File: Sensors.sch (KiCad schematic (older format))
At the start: 0 parts

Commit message: Added Polyfuses and replace diodes
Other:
- note removed: "Gniazdo USB B\nSWD\nUART"
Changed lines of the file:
@@
 $Descr A4 11693 8268
 encoding utf-8
-Sheet 7 10
+Sheet 10 10
 Title ""
 Date ""
@@
 Comment4 ""
 $EndDescr
-Text Notes 1300 1250 0    50   ~ 0
-Gniazdo USB B\nSWD\nUART
 $EndSCHEMATC

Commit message: Numbering and finishing the schematic
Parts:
- added C66: 0.1uF, symbol Device:C
- added R72, R73: 2.2kΩ, symbol Device:R
- added U10: SHTC3, footprints:DFN-4-1EP_2x2mm_P1mm_EP0.7x1.6mm, symbol Library:SHTC3
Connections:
- new net +3V3: C66.1, R72.1, R73.1, U10.1 (VDD)
- new net GND: C66.2, U10.4 (VSS)
- new net I2C_SCL: R73.2, U10.2 (SCL)
- new net I2C_SDA: R72.2, U10.3 (SDA)
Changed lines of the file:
@@
 Comment4 ""
 $EndDescr
+$Comp
+L Library:SHTC3 U10
+U 1 1 5E1916D2
+P 3250 2450
+F 0 "U10" H 3000 2700 50  0000 L CNN
+F 1 "SHTC3" H 3250 2700 50  0000 L CNN
+F 2 "footprints:DFN-4-1EP_2x2mm_P1mm_EP0.7x1.6mm" H 3050 2200 50  0001 C CNN
+F 3 "" H 3050 2200 50  0001 C CNN
+	1    3250 2450
+	1    0    0    -1
+$EndComp
+$Comp
+L Device:C C66
+U 1 1 5E15E1F1
+P 3900 2450
+F 0 "C66" H 4015 2496 50  0000 L CNN
+F 1 "0.1uF" H 4015 2405 50  0000 L CNN
+F 2 "" H 3938 2300 50  0001 C CNN
+F 3 "~" H 3900 2450 50  0001 C CNN
+	1    3900 2450
+	1    0    0    -1
+$EndComp
+$Comp
+L power:GND #PWR0177
+U 1 1 5E15EB06
+P 3900 2700
+F 0 "#PWR0177" H 3900 2450 50  0001 C CNN
+F 1 "GND" H 3905 2527 50  0000 C CNN
+F 2 "" H 3900 2700 50  0001 C CNN
+F 3 "" H 3900 2700 50  0001 C CNN
+	1    3900 2700
+	1    0    0    -1
+$EndComp
+$Comp
+L power:+3.3V #PWR0176
+U 1 1 5E15FDB5
+P 3900 1650
+F 0 "#PWR0176" H 3900 1500 50  0001 C CNN
+F 1 "+3.3V" H 3915 1823 50  0000 C CNN
+F 2 "" H 3900 1650 50  0001 C CNN
+F 3 "" H 3900 1650 50  0001 C CNN
+	1    3900 1650
+	1    0    0    -1
+$EndComp
+Wire Wire Line
+	3900 1650 3900 1750
+Wire Wire Line
+	3900 2250 3700 2250
+Wire Wire Line
+	3700 2250 3700 2400
+Wire Wire Line
+	3700 2400 3650 2400
+Connection ~ 3900 2250
+Wire Wire Line
+	3900 2250 3900 2300
+Wire Wire Line
+	3650 2500 3700 2500
+Wire Wire Line
+	3700 2500 3700 2650
+Wire Wire Line
+	3700 2650 3900 2650
+Wire Wire Line
+	3900 2650 3900 2600
+Wire Wire Line
+	3900 2700 3900 2650
+Connection ~ 3900 2650
+Wire Wire Line
+	2850 2400 2600 2400
+Wire Wire Line
+	2850 2500 2250 2500
+Text GLabel 2100 2400 0    50   Input ~ 0
+I2C_SCL
+Text GLabel 2100 2500 0    50   BiDi ~ 0
+I2C_SDA
+$Comp
+L Device:R R?
+U 1 1 5E1C6F9E
+P 2600 2100
+AR Path="/5E91D7CC/5E1C6F9E" Ref="R?"  Part="1"
+AR Path="/5E91D96F/5E1C6F9E" Ref="R?"  Part="1"
+AR Path="/5E1B3A8F/5E1C6F9E" Ref="R73"  Part="1"
+F 0 "R73" H 2670 2146 50  0000 L CNN
+F 1 "2.2kΩ" H 2670 2055 50  0000 L CNN
+F 2 "" V 2530 2100 50  0001 C CNN
+F 3 "~" H 2600 2100 50  0001 C CNN
+	1    2600 2100
+	1    0    0    -1
+$EndComp
+$Comp
+L Device:R R?
+U 1 1 5E1C6FA4
+P 2250 2100
+AR Path="/5E91D7CC/5E1C6FA4" Ref="R?"  Part="1"
+AR Path="/5E91D96F/5E1C6FA4" Ref="R?"  Part="1"
+AR Path="/5E1B3A8F/5E1C6FA4" Ref="R72"  Part="1"
+F 0 "R72" H 2320 2146 50  0000 L CNN
+F 1 "2.2kΩ" H 2320 2055 50  0000 L CNN
+F 2 "" V 2180 2100 50  0001 C CNN
+F 3 "~" H 2250 2100 50  0001 C CNN
+	1    2250 2100
+	1    0    0    -1
+$EndComp
+Wire Wire Line
+	2250 2250 2250 2500
+Wire Wire Line
+	2600 1950 2600 1750
+Wire Wire Line
+	2600 1750 2250 1750
+Wire Wire Line
+	2250 1750 2250 1950
+Connection ~ 2600 1750
+Connection ~ 2250 2500
+Wire Wire Line
+	2250 2500 2100 2500
+Wire Wire Line
+	2600 2250 2600 2400
+Connection ~ 2600 2400
+Wire Wire Line
+	2600 2400 2100 2400
+Wire Wire Line
+	2600 1750 3900 1750
+Connection ~ 3900 1750
+Wire Wire Line
+	3900 1750 3900 2250
 $EndSCHEMATC

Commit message: Shematic almost finished, BOM in KiCad 3/4 finished
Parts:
- C68: renamed from C66; footprint (none) -> Capacitor_SMD:C_0603_1608Metric; Cena (none) -> 0.05982; Model (none) -> CL10B104KB8NNNC; Napięcie (none) -> 50V; Producent (none) -> SAMSUNG; Tolerancja (none) -> 10%; Typ (none) -> SMD
- R72, R73: footprint (none) -> Resistor_SMD:R_0603_1608Metric
- U10: Cena (none) -> 7.2; Link (none) -> https://www.tme.eu/pl/details/shtc3/czujniki-wilgotnosci/se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; Model (none) -> SHTC3; Opis (none) -> Czujnik: temperatury i wilgotności; Zakres: 0÷100% RH; -0,3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; Producent (none) -> SENSIRION; Typ (none) -> SMD
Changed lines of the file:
@@
 F 2 "footprints:DFN-4-1EP_2x2mm_P1mm_EP0.7x1.6mm" H 3050 2200 50  0001 C CNN
 F 3 "" H 3050 2200 50  0001 C CNN
+F 4 "7.2" H 3250 2450 50  0001 C CNN "Cena"
+F 5 "https://www.tme.eu/pl/details/shtc3/czujniki-wilgotnosci/sensirion/3-000-047/" H 3250 2450 50  0001 C CNN "Link"
+F 6 "SHTC3" H 3250 2450 50  0001 C CNN "Model"
+F 7 "Czujnik: temperatury i wilgotności; Zakres: 0÷100% RH; -0,3÷4VDC" H 3250 2450 50  0001 C CNN "Opis"
+F 8 "SENSIRION" H 3250 2450 50  0001 C CNN "Producent"
+F 9 "SMD" H 3250 2450 50  0001 C CNN "Typ"
 	1    3250 2450
 	1    0    0    -1
 $EndComp
 $Comp
-L Device:C C66
+L Device:C C68
 U 1 1 5E15E1F1
 P 3900 2450
-F 0 "C66" H 4015 2496 50  0000 L CNN
+F 0 "C68" H 4015 2496 50  0000 L CNN
 F 1 "0.1uF" H 4015 2405 50  0000 L CNN
-F 2 "" H 3938 2300 50  0001 C CNN
+F 2 "Capacitor_SMD:C_0603_1608Metric" H 3938 2300 50  0001 C CNN
 F 3 "~" H 3900 2450 50  0001 C CNN
+F 4 "0.05982" H 3900 2450 50  0001 C CNN "Cena"
+F 5 "CL10B104KB8NNNC " H 3900 2450 50  0001 C CNN "Model"
+F 6 "50V" H 3900 2450 50  0001 C CNN "Napięcie"
+F 7 "SAMSUNG" H 3900 2450 50  0001 C CNN "Producent"
+F 8 "10%" H 3900 2450 50  0001 C CNN "Tolerancja"
+F 9 "SMD" H 3900 2450 50  0001 C CNN "Typ"
 	1    3900 2450
 	1    0    0    -1
@@
 F 0 "R73" H 2670 2146 50  0000 L CNN
 F 1 "2.2kΩ" H 2670 2055 50  0000 L CNN
-F 2 "" V 2530 2100 50  0001 C CNN
+F 2 "Resistor_SMD:R_0603_1608Metric" V 2530 2100 50  0001 C CNN
 F 3 "~" H 2600 2100 50  0001 C CNN
 	1    2600 2100
@@
 F 0 "R72" H 2320 2146 50  0000 L CNN
 F 1 "2.2kΩ" H 2320 2055 50  0000 L CNN
-F 2 "" V 2180 2100 50  0001 C CNN
+F 2 "Resistor_SMD:R_0603_1608Metric" V 2180 2100 50  0001 C CNN
 F 3 "~" H 2250 2100 50  0001 C CNN
 	1    2250 2100

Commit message: BOM in KiCad almost finished, genereated NETLIST, create PCB
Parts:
- R72, R73: Cena (none) -> 0.04651; Typ (none) -> SMD
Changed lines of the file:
@@
 F 2 "Resistor_SMD:R_0603_1608Metric" V 2530 2100 50  0001 C CNN
 F 3 "~" H 2600 2100 50  0001 C CNN
+F 4 "0.04651" H 2600 2100 50  0001 C CNN "Cena"
+F 5 "SMD" H 2600 2100 50  0001 C CNN "Typ"
 	1    2600 2100
 	1    0    0    -1
@@
 F 2 "Resistor_SMD:R_0603_1608Metric" V 2180 2100 50  0001 C CNN
 F 3 "~" H 2250 2100 50  0001 C CNN
+F 4 "0.04651" H 2250 2100 50  0001 C CNN "Cena"
+F 5 "SMD" H 2250 2100 50  0001 C CNN "Typ"
 	1    2250 2100
 	1    0    0    -1

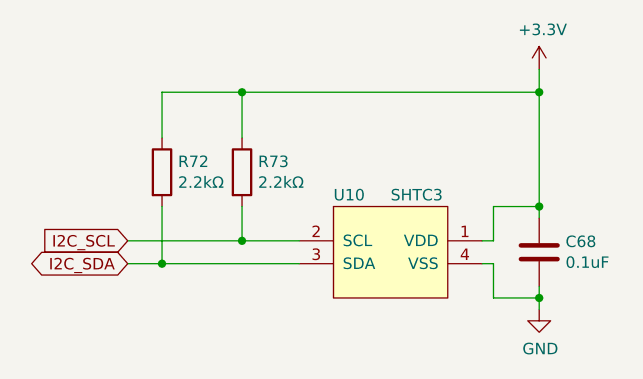
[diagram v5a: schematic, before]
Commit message: Improve Emergency, Added TVS diodes
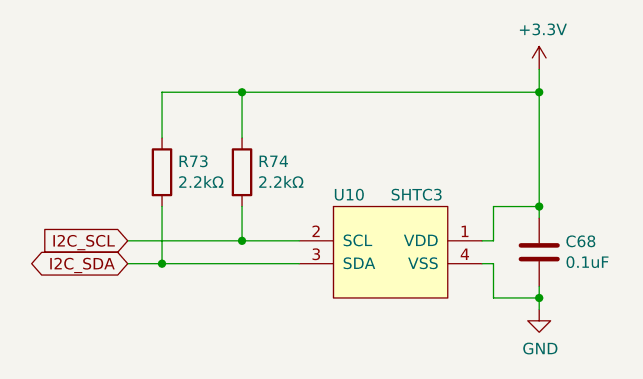
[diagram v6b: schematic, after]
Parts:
- renumbered R72 to R73, R73 to R74
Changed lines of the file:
@@
 $EndComp
 $Comp
-L power:GND #PWR0177
+L power:GND #PWR0176
 U 1 1 5E15EB06
 P 3900 2700
-F 0 "#PWR0177" H 3900 2450 50  0001 C CNN
+F 0 "#PWR0176" H 3900 2450 50  0001 C CNN
 F 1 "GND" H 3905 2527 50  0000 C CNN
 F 2 "" H 3900 2700 50  0001 C CNN
@@
 $EndComp
 $Comp
-L power:+3.3V #PWR0176
+L power:+3.3V #PWR0175
 U 1 1 5E15FDB5
 P 3900 1650
-F 0 "#PWR0176" H 3900 1500 50  0001 C CNN
+F 0 "#PWR0175" H 3900 1500 50  0001 C CNN
 F 1 "+3.3V" H 3915 1823 50  0000 C CNN
 F 2 "" H 3900 1650 50  0001 C CNN
@@
 AR Path="/5E91D7CC/5E1C6F9E" Ref="R?"  Part="1"
 AR Path="/5E91D96F/5E1C6F9E" Ref="R?"  Part="1"
-AR Path="/5E1B3A8F/5E1C6F9E" Ref="R73"  Part="1"
-F 0 "R73" H 2670 2146 50  0000 L CNN
+AR Path="/5E1B3A8F/5E1C6F9E" Ref="R74"  Part="1"
+F 0 "R74" H 2670 2146 50  0000 L CNN
 F 1 "2.2kΩ" H 2670 2055 50  0000 L CNN
 F 2 "Resistor_SMD:R_0603_1608Metric" V 2530 2100 50  0001 C CNN
@@
 AR Path="/5E91D7CC/5E1C6FA4" Ref="R?"  Part="1"
 AR Path="/5E91D96F/5E1C6FA4" Ref="R?"  Part="1"
-AR Path="/5E1B3A8F/5E1C6FA4" Ref="R72"  Part="1"
-F 0 "R72" H 2320 2146 50  0000 L CNN
+AR Path="/5E1B3A8F/5E1C6FA4" Ref="R73"  Part="1"
+F 0 "R73" H 2320 2146 50  0000 L CNN
 F 1 "2.2kΩ" H 2320 2055 50  0000 L CNN
 F 2 "Resistor_SMD:R_0603_1608Metric" V 2180 2100 50  0001 C CNN

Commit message: Added 12V regulator, aditional input, outputs, improved inputs ESD
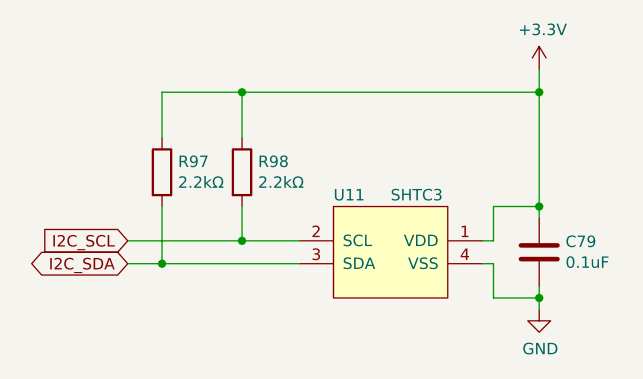
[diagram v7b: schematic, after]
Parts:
- renumbered C68 to C79, R73 to R97, R74 to R98, U10 to U11
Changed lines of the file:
@@
 $EndDescr
 $Comp
-L Library:SHTC3 U10
+L Library:SHTC3 U11
 U 1 1 5E1916D2
 P 3250 2450
-F 0 "U10" H 3000 2700 50  0000 L CNN
+F 0 "U11" H 3000 2700 50  0000 L CNN
 F 1 "SHTC3" H 3250 2700 50  0000 L CNN
 F 2 "footprints:DFN-4-1EP_2x2mm_P1mm_EP0.7x1.6mm" H 3050 2200 50  0001 C CNN
@@
 $EndComp
 $Comp
-L Device:C C68
+L Device:C C79
 U 1 1 5E15E1F1
 P 3900 2450
-F 0 "C68" H 4015 2496 50  0000 L CNN
+F 0 "C79" H 4015 2496 50  0000 L CNN
 F 1 "0.1uF" H 4015 2405 50  0000 L CNN
 F 2 "Capacitor_SMD:C_0603_1608Metric" H 3938 2300 50  0001 C CNN
@@
 $EndComp
 $Comp
-L power:GND #PWR0176
+L power:GND #PWR0217
 U 1 1 5E15EB06
 P 3900 2700
-F 0 "#PWR0176" H 3900 2450 50  0001 C CNN
+F 0 "#PWR0217" H 3900 2450 50  0001 C CNN
 F 1 "GND" H 3905 2527 50  0000 C CNN
 F 2 "" H 3900 2700 50  0001 C CNN
@@
 $EndComp
 $Comp
-L power:+3.3V #PWR0175
+L power:+3.3V #PWR0216
 U 1 1 5E15FDB5
 P 3900 1650
-F 0 "#PWR0175" H 3900 1500 50  0001 C CNN
+F 0 "#PWR0216" H 3900 1500 50  0001 C CNN
 F 1 "+3.3V" H 3915 1823 50  0000 C CNN
 F 2 "" H 3900 1650 50  0001 C CNN
@@
 AR Path="/5E91D7CC/5E1C6F9E" Ref="R?"  Part="1"
 AR Path="/5E91D96F/5E1C6F9E" Ref="R?"  Part="1"
-AR Path="/5E1B3A8F/5E1C6F9E" Ref="R74"  Part="1"
-F 0 "R74" H 2670 2146 50  0000 L CNN
+AR Path="/5E1B3A8F/5E1C6F9E" Ref="R98"  Part="1"
+F 0 "R98" H 2670 2146 50  0000 L CNN
 F 1 "2.2kΩ" H 2670 2055 50  0000 L CNN
 F 2 "Resistor_SMD:R_0603_1608Metric" V 2530 2100 50  0001 C CNN
@@
 AR Path="/5E91D7CC/5E1C6FA4" Ref="R?"  Part="1"
 AR Path="/5E91D96F/5E1C6FA4" Ref="R?"  Part="1"
-AR Path="/5E1B3A8F/5E1C6FA4" Ref="R73"  Part="1"
-F 0 "R73" H 2320 2146 50  0000 L CNN
+AR Path="/5E1B3A8F/5E1C6FA4" Ref="R97"  Part="1"
+F 0 "R97" H 2320 2146 50  0000 L CNN
 F 1 "2.2kΩ" H 2320 2055 50  0000 L CNN
 F 2 "Resistor_SMD:R_0603_1608Metric" V 2180 2100 50  0001 C CNN

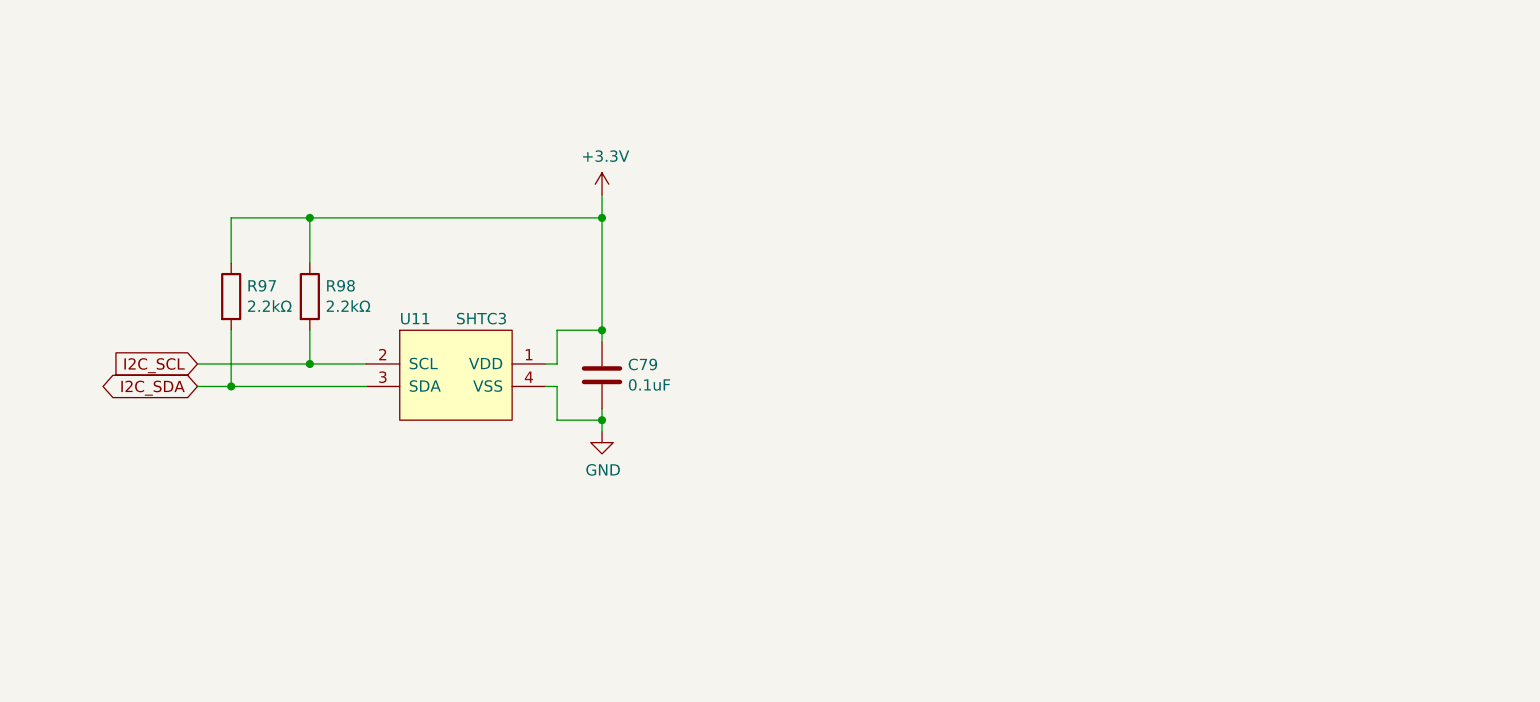
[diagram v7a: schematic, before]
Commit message: Added analog input
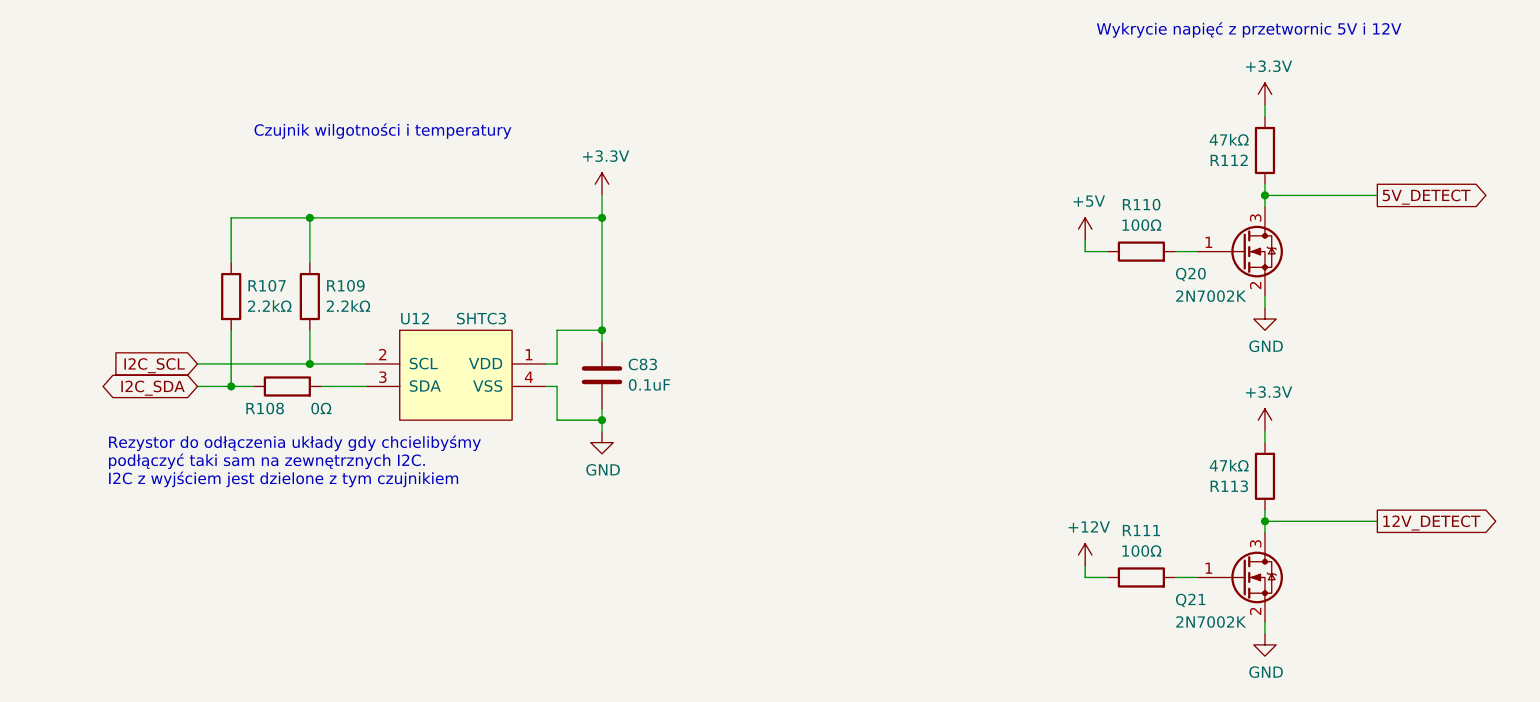
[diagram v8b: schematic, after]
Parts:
- added Q20, Q21: 2N7002K, Package_TO_SOT_SMD:SOT-23, symbol Transistor_FET:2N7002K
- added R108: 0Ω, Resistor_SMD:R_0603_1608Metric, symbol Device:R
- added R110, R111: 100Ω, Resistor_SMD:R_0603_1608Metric, symbol Device:R
- added R112, R113: 47kΩ, Resistor_SMD:R_0603_1608Metric, symbol Device:R
- renumbered C79 to C83, R97 to R107, R98 to R109, U11 to U12
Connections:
- net +3V3: now also R112.2, R113.2
- net GND: now also Q20.2 (S), Q21.2 (S)
- net I2C_SDA: now also R108.1; no longer U12.3 (SDA)
- new net: R108.2, U12.3 (SDA)
- new net: Q20.1 (G), R110.2
- new net: Q21.1 (G), R111.2
- new net +12V: R111.1
- new net +5V: R110.1
- new net 12V_DETECT: Q21.3 (D), R113.1
- new net 5V_DETECT: Q20.3 (D), R112.1
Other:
- note added: "Czujnik wilgotności i temperatury"
- note added: "Rezystor do odłączenia układy gdy chcielibyśmy\npodłączyć taki sam na zewnętrznych I2C.\nI2C z wyjściem jest dzielone z tym czujnikiem"
- note added: "Wykrycie napięć z przetwornic 5V i 12V"
